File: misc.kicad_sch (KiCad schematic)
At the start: 12 parts

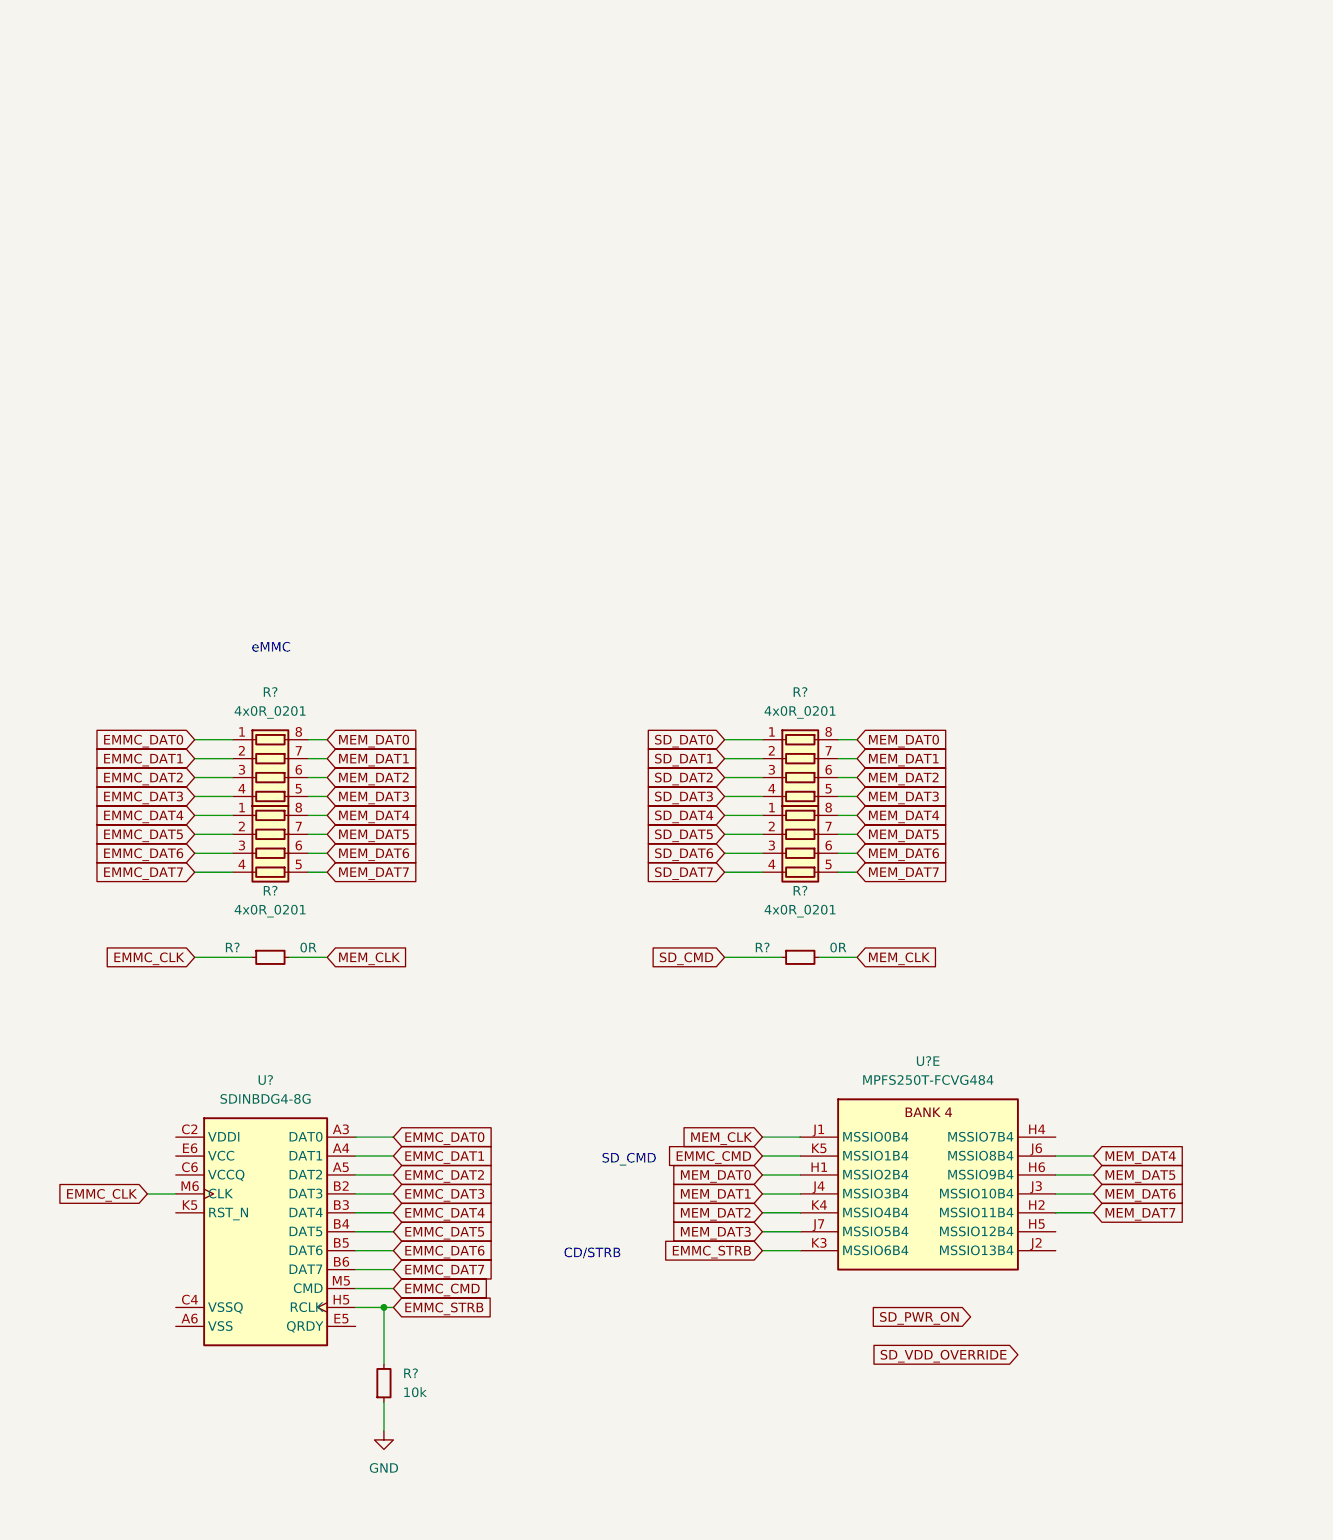
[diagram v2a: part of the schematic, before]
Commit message: [#54013] Add eMMC pullup resistors
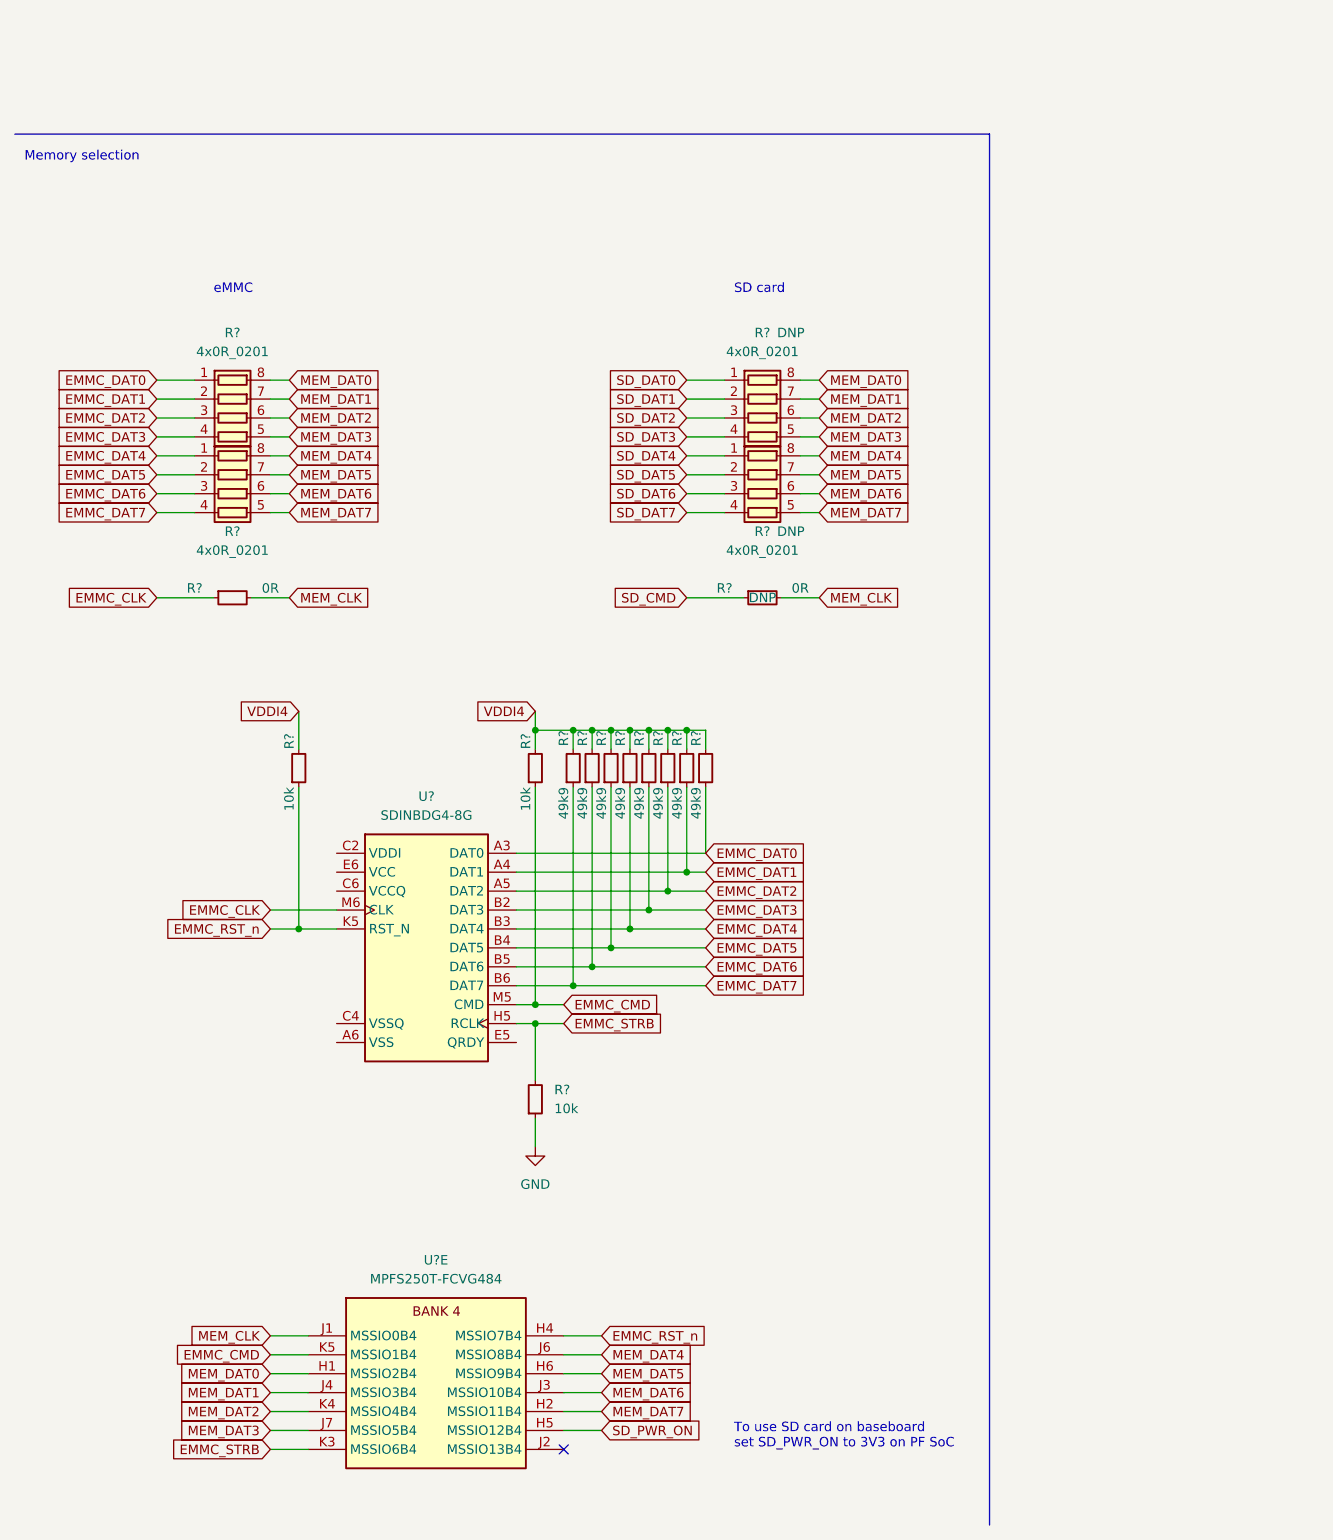
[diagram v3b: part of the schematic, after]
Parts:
- added R? (x8): R_49k9_0402, antmicro-footprints:R_0402_1005Metric, symbol antmicroResistors0402:R_49k9_0402
- added R? (x2): R_10k_0402, antmicro-footprints:R_0402_1005Metric, symbol antmicroResistors0402:R_10k_0402
- R? (x3): DNP (none) -> DNP
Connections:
- net EMMC_CMD: now also R?.1
- net EMMC_DAT0: now also R?.1
- net EMMC_DAT1: now also R?.1
- net EMMC_DAT2: now also R?.1
- net EMMC_DAT3: now also R?.1
- net EMMC_DAT4: now also R?.1
- net EMMC_DAT5: now also R?.1
- net EMMC_DAT6: now also R?.1
- net EMMC_DAT7: now also R?.1
- net SD_PWR_ON: now also U?.H5 (MSSIO12B4)
- net EMMC_RST_n: now reaches U?.H4 (MSSIO7B4)
- net EMMC_RST_n: now also U?.K5 (RST_N), R?.1
- new net VDDI4: R?.2, R?.2, R?.2, R?.2, R?.2, R?.2, R?.2, R?.2, R?.2, R?.2
- no-connect marks 0 -> 1
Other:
- note added: "Memory selection"
- note added: "SD card"
- note added: "To use SD card on baseboard set SD_PWR_ON to 3V3 on PF SoC"
- note removed: "CD/STRB"
- note removed: "SD_CMD"
- moved on the sheet: R?, U?, U?E

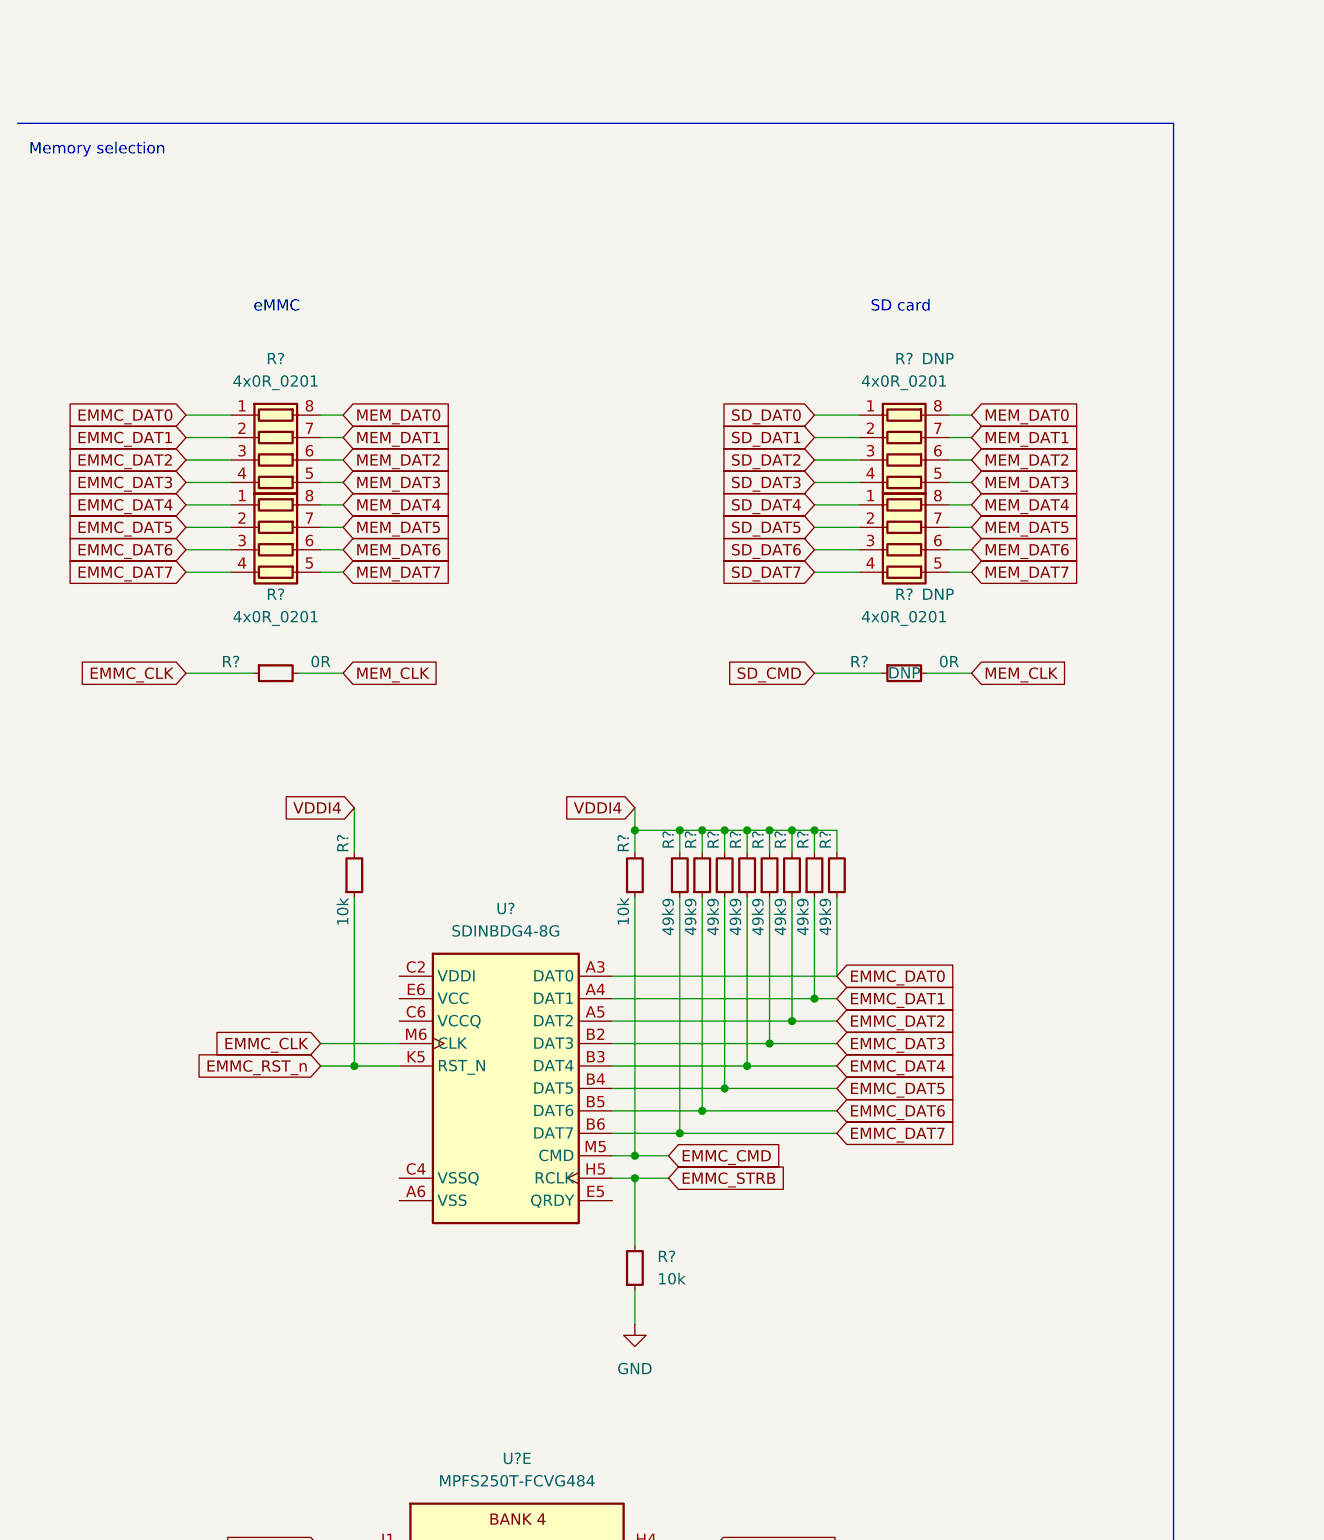
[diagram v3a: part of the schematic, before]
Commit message: [#54013] Add eMMC decoupling capacitors
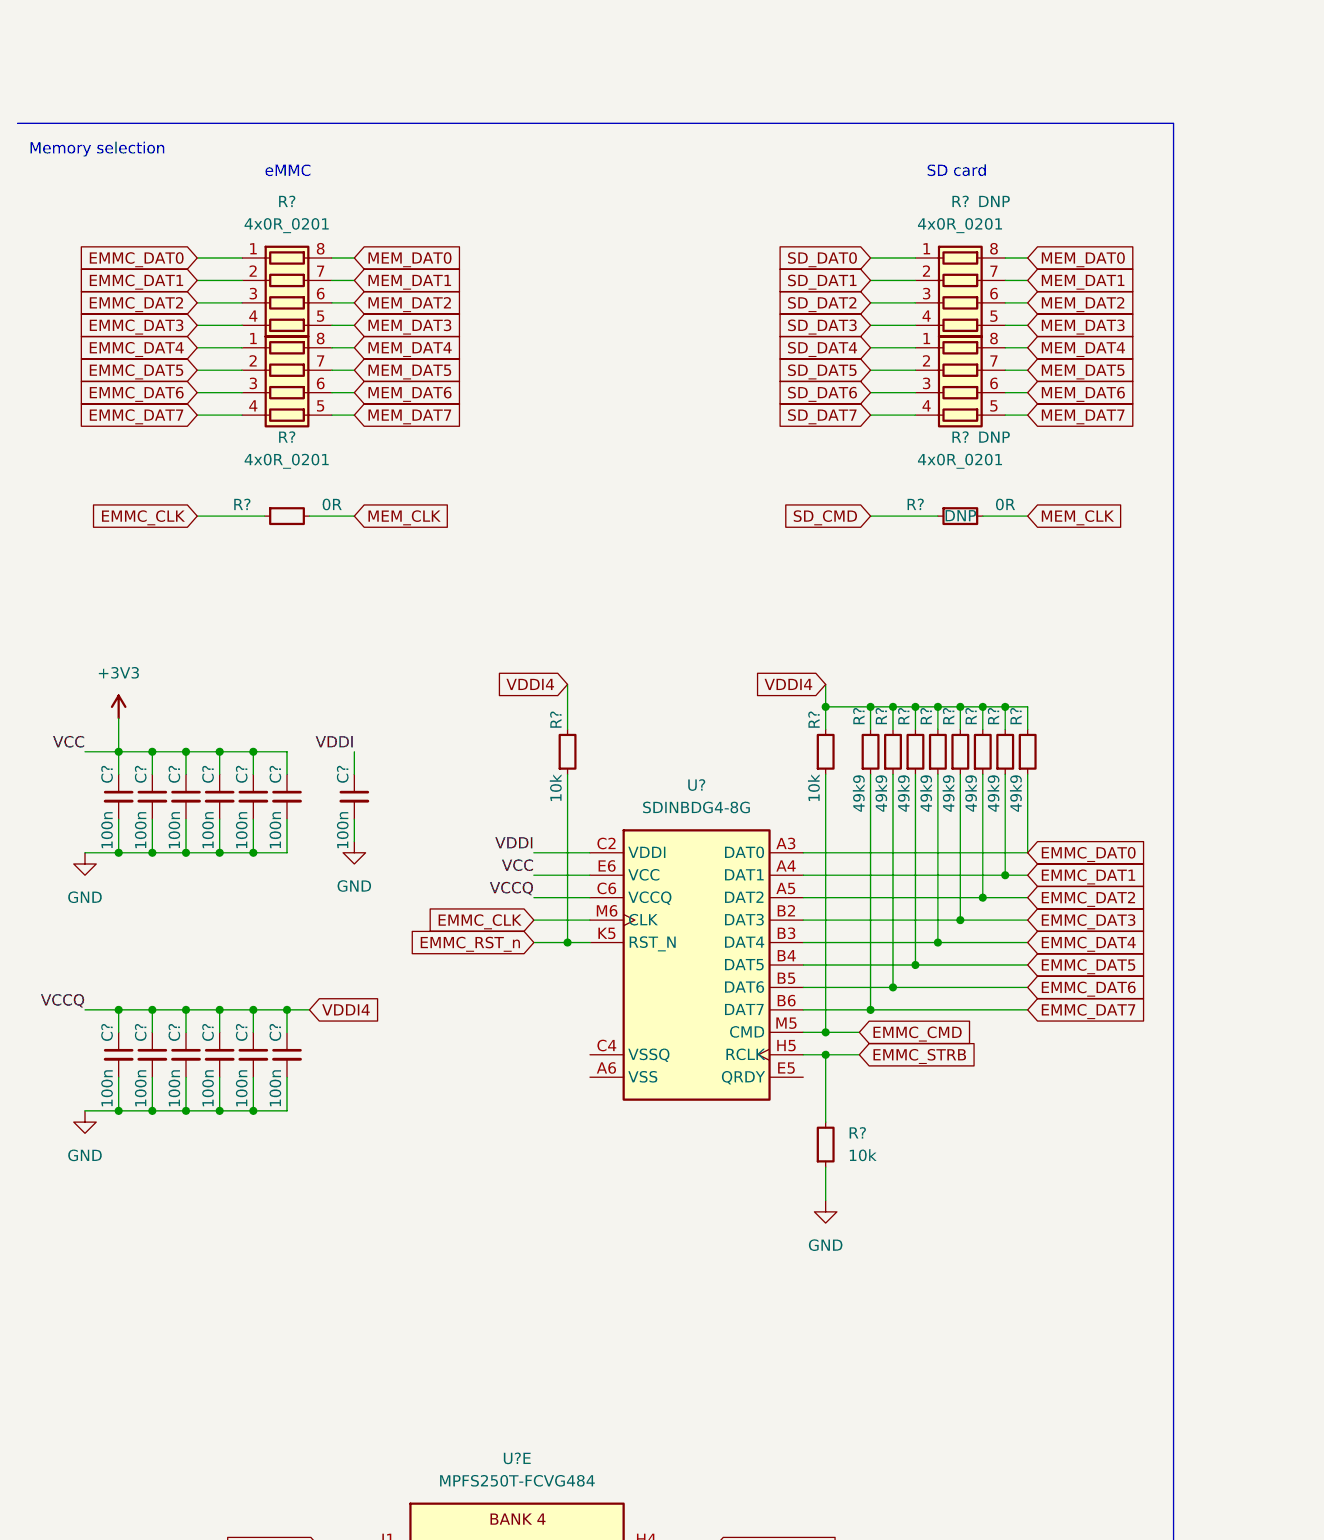
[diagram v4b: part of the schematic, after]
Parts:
- added C? (x13): C_100n_25V_0402, antmicro-footprints:C_0402_1005Metric, symbol antmicroCapacitors0402:C_100n_25V_0402
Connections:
- net GND: now also C?.2, C?.2, C?.2, C?.2, C?.2, C?.2, C?.2, C?.2, C?.2, C?.2, C?.2, C?.2, C?.2
- net VDDI4: now also U?.C6 (VCCQ), U?.M4 (VCCQ), U?.N4 (VCCQ), U?.P3 (VCCQ), U?.P5 (VCCQ), C?.1, C?.1, C?.1, C?.1, C?.1, C?.1
- net VDDI: now reaches U?.C2 (VDDI)
- net VDDI: now also C?.1
- net +3V3: now reaches U?.E6 (VCC), U?.F5 (VCC), U?.J10 (VCC), U?.K9 (VCC)
- net +3V3: now also C?.1, C?.1, C?.1, C?.1, C?.1, C?.1
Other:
- moved on the sheet: R?, U?

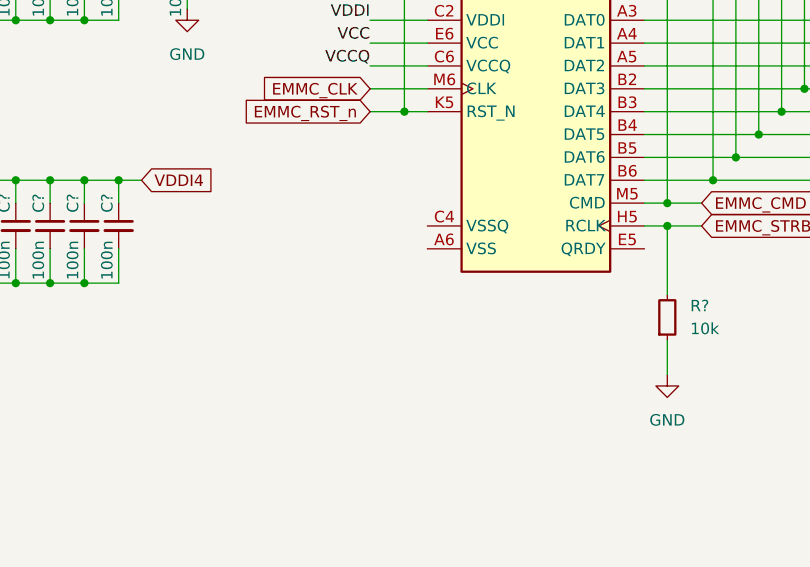
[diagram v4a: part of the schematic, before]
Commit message: [#54013] Ground VSS pins on eMMC flash
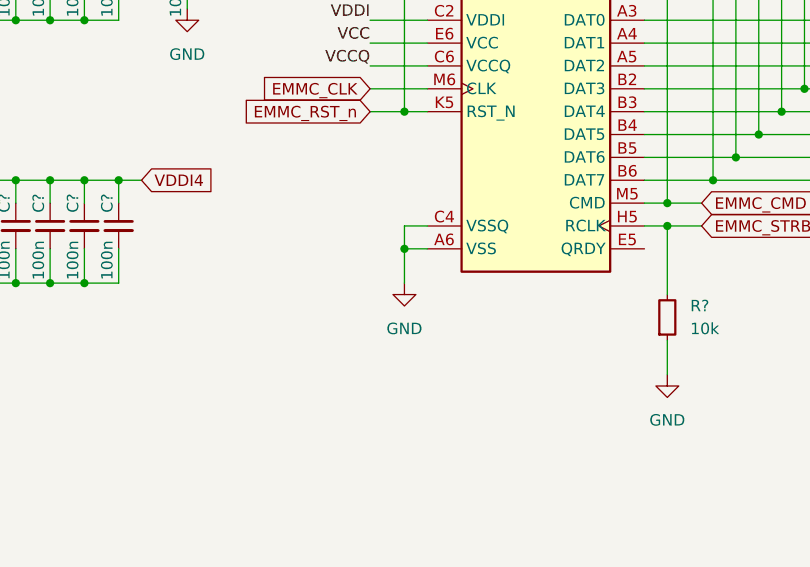
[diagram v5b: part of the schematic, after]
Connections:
- net GND: now also U?.A6 (VSS), U?.C4 (VSSQ), U?.E7 (VSS), U?.G5 (VSS), U?.H10 (VSS), U?.J5 (VSS), U?.K8 (VSS), U?.N2 (VSSQ), U?.N5 (VSSQ), U?.P4 (VSSQ), U?.P6 (VSSQ)
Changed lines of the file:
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@@
   (junction (at 115.57 163.83) (diameter 0) (color 0 0 0 0)
+  )
+  (junction (at 73.66 205.74) (diameter 0) (color 0 0 0 0)
   )
   (junction (at 26.67 168.91) (diameter 0) (color 0 0 0 0)
@@
     (stroke (width 0) (type default) (color 0 0 0 0))
   )
+  (wire (pts (xy 73.66 205.74) (xy 73.66 209.55))
+    (stroke (width 0) (type default) (color 0 0 0 0))
+  )
   (wire (pts (xy 323.85 172.72) (xy 328.93 172.72))
     (stroke (width 0) (type default) (color 0 0 0 0))
@@
     (stroke (width 0) (type default) (color 0 0 0 0))
   )
+  (wire (pts (xy 76.2 203.2) (xy 73.66 203.2))
+    (stroke (width 0) (type default) (color 0 0 0 0))
+  )
   (wire (pts (xy 100.33 182.88) (xy 123.19 182.88))
     (stroke (width 0) (type default) (color 0 0 0 0))
@@
     (stroke (width 0) (type default) (color 0 0 0 0))
   )
+  (wire (pts (xy 73.66 203.2) (xy 73.66 205.74))
+    (stroke (width 0) (type default) (color 0 0 0 0))
+  )
   (wire (pts (xy 123.19 115.57) (xy 125.73 115.57))
     (stroke (width 0) (type default) (color 0 0 0 0))
@@
   )
   (wire (pts (xy 38.1 168.91) (xy 38.1 171.45))
+    (stroke (width 0) (type default) (color 0 0 0 0))
+  )
+  (wire (pts (xy 73.66 205.74) (xy 76.2 205.74))
     (stroke (width 0) (type default) (color 0 0 0 0))
   )
@@
     (pin "2")
   )
+  (symbol (lib_id "antmicropower:GND") (at 73.66 209.55 0) (unit 1)
+    (in_bom yes) (on_board yes) (fields_autoplaced)
+    (property "Reference" "#PWR?" (id 0) (at 82.55 212.09 0)
+      (effects (font (size 1.27 1.27) (thickness 0.15)) (justify left bottom) hide)
+    )
+    (property "Value" "GND" (id 1) (at 73.66 214.63 0)
+      (effects (font (size 1.27 1.27) (thickness 0.15)))
+    )
+    (property "Footprint" "" (id 2) (at 82.55 217.17 0)
+      (effects (font (size 1.27 1.27) (thickness 0.15)) (justify left bottom) hide)
+    )
+    (property "Datasheet" "" (id 3) (at 82.55 222.25 0)
+      (effects (font (size 1.27 1.27) (thickness 0.15)) (justify left bottom) hide)
+    )
+    (property "Author" "Antmicro" (id 4) (at 82.55 217.17 0)
+      (effects (font (size 1.27 1.27) (thickness 0.15)) (justify left bottom) hide)
+    )
+    (property "License" "Apache-2.0" (id 5) (at 82.55 219.71 0)
+      (effects (font (size 1.27 1.27) (thickness 0.15)) (justify left bottom) hide)
+    )
+    (pin "1")
+  )
   (symbol (lib_id "antmicropower:+3V3") (at 22.86 165.1 0) (unit 1)
